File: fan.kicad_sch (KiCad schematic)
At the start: 9 parts, among them J6 Conn_01x04, U11 EMC2101

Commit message: migrated over lots of bitaxe parts to blockaxe
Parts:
- J6: footprint bitaxe:470531000 -> blockaxe:470531000
- U11: symbol bitaxe:EMC2101 -> blockaxe:EMC2101
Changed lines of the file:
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@@
       (effects (font (size 1.27 1.27)) hide)
     )
-    (property "Footprint" "bitaxe:470531000" (at 177.8 107.95 0)
+    (property "Footprint" "blockaxe:470531000" (at 177.8 107.95 0)
       (effects (font (size 1.27 1.27)) hide)
     )
@@
     )
   )
-  (symbol (lib_id "bitaxe:EMC2101") (at 139.065 72.39 0) (unit 1)
+  (symbol (lib_id "blockaxe:EMC2101") (at 139.065 72.39 0) (unit 1)
     (in_bom yes) (on_board yes) (dnp no)
     (property "Reference" "U11" (at 147.955 63.5 0)

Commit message: finished routing. switched back to THT barrel
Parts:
- TP13, TP14: footprint TestPoint:TestPoint_Pad_D1.5mm -> TestPoint:TestPoint_Pad_D1.0mm
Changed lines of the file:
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@@
       (effects (font (size 1.27 1.27)) (justify left) hide)
     )
-    (property "Footprint" "TestPoint:TestPoint_Pad_D1.5mm" (at 129.54 110.49 0)
+    (property "Footprint" "TestPoint:TestPoint_Pad_D1.0mm" (at 129.54 110.49 0)
       (effects (font (size 1.27 1.27)) hide)
     )
@@
       (effects (font (size 1.27 1.27)) (justify left) hide)
     )
-    (property "Footprint" "TestPoint:TestPoint_Pad_D1.5mm" (at 163.195 107.95 0)
+    (property "Footprint" "TestPoint:TestPoint_Pad_D1.0mm" (at 163.195 107.95 0)
       (effects (font (size 1.27 1.27)) hide)
     )

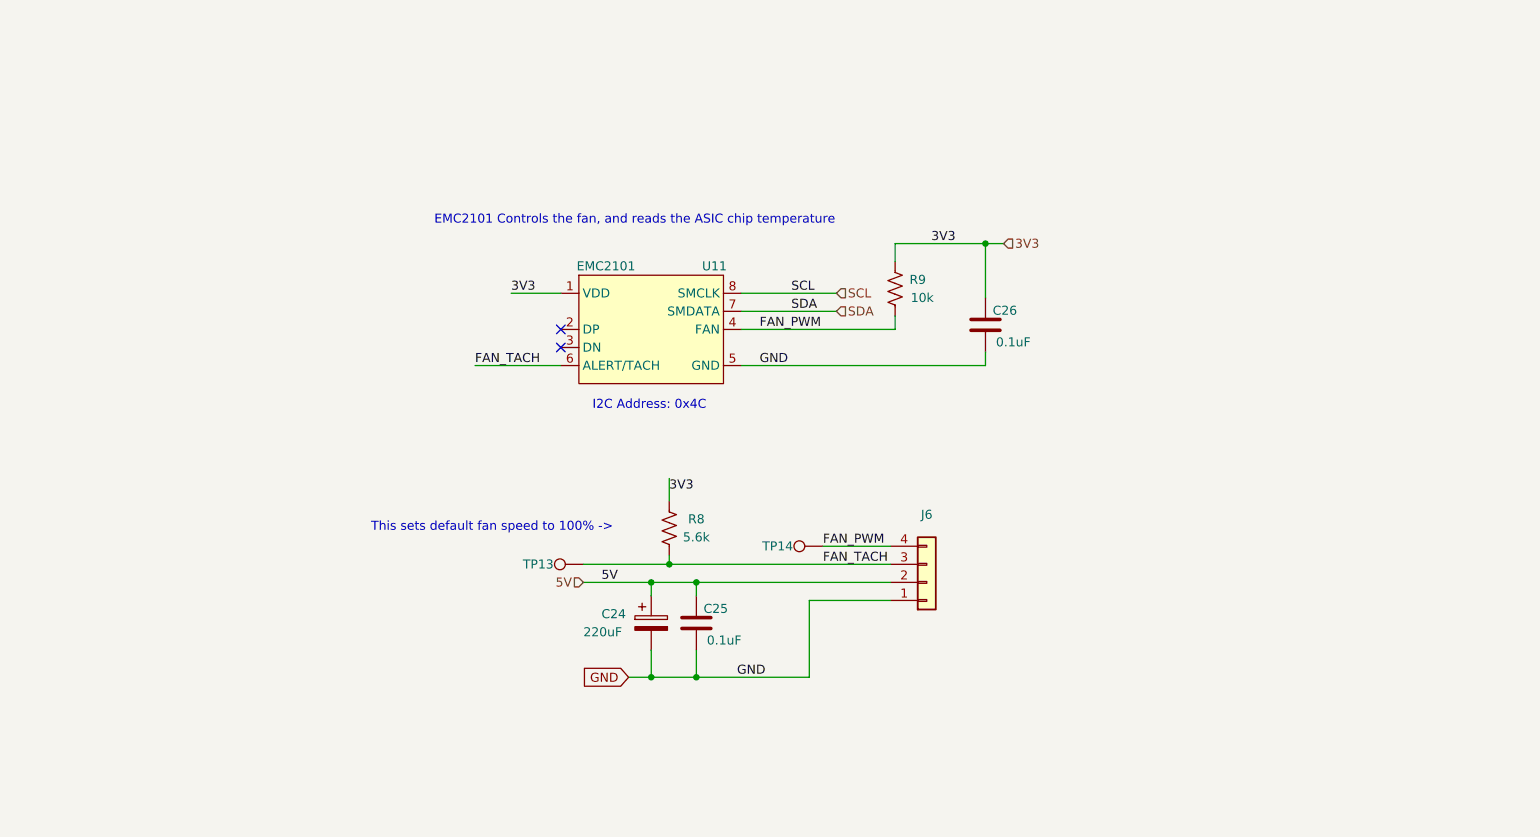
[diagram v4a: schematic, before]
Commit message: switch to bitaxeAura/GT base
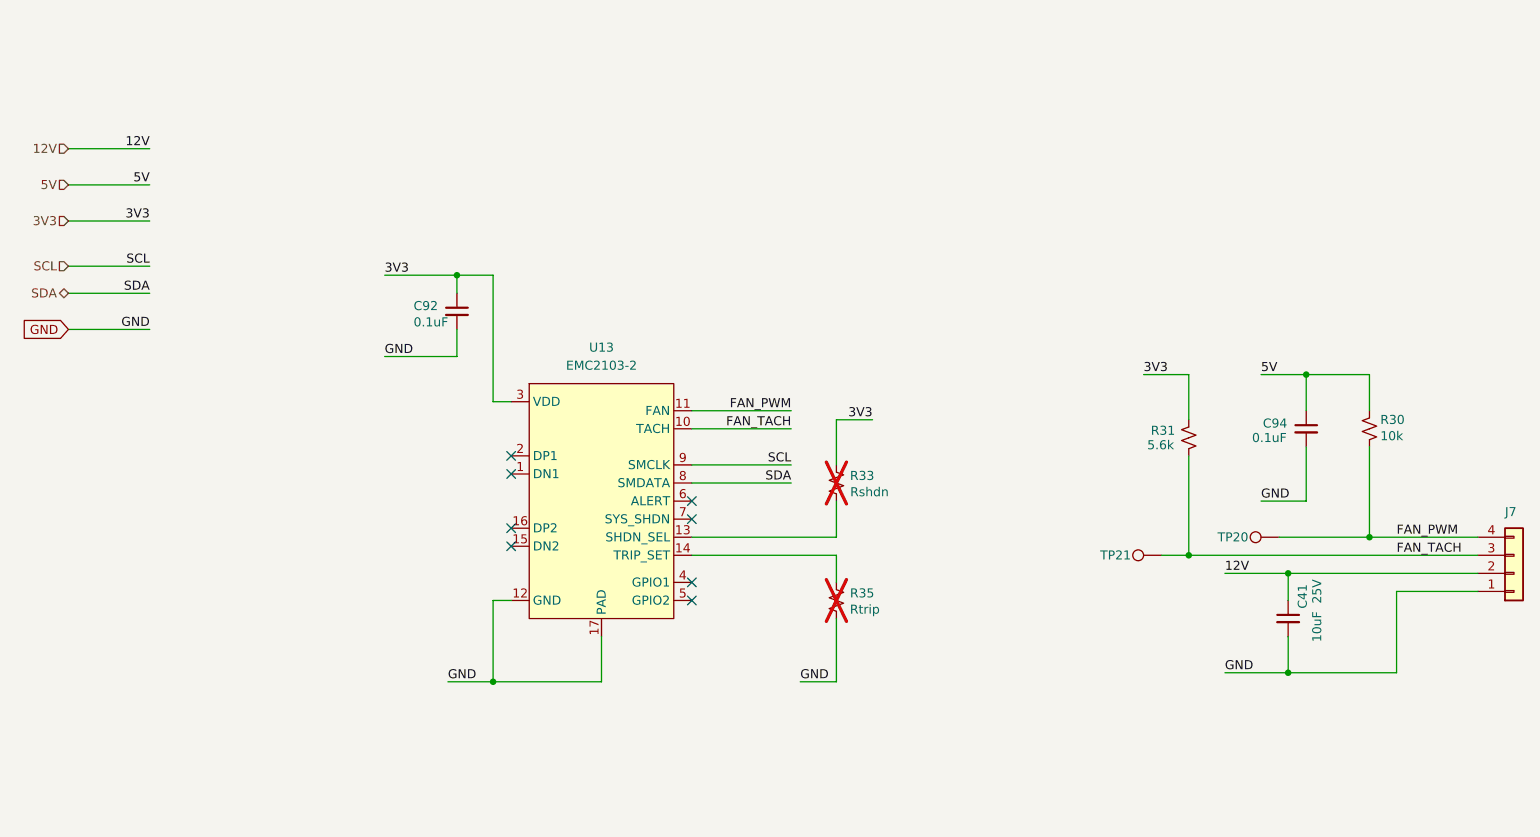
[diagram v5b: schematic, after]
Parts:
- removed C24: 220uF, Capacitor_SMD:CP_Elec_6.3x7.7, symbol Device:C_Polarized
- removed C25, C26: 0.1uF, Capacitor_SMD:C_0402_1005Metric, symbol Device:C
- removed J6: Conn_01x04, blockaxe:470531000, symbol Connector_Generic:Conn_01x04
- removed R8: 5.6k, Resistor_SMD:R_0402_1005Metric, symbol Device:R_US
- removed R9: 10k, Resistor_SMD:R_0402_1005Metric, symbol Device:R_US
- removed TP13, TP14: TestPoint, TestPoint:TestPoint_Pad_D1.0mm, symbol Connector:TestPoint
- removed U11: EMC2101, Package_SO:TSSOP-8_3x3mm_P0.65mm, symbol blockaxe:EMC2101
- added C41: 10uF, Capacitor_SMD:C_0603_1608Metric, symbol Device:C_Small
- added C92, C94: 0.1uF, Capacitor_SMD:C_0402_1005Metric, symbol Device:C_Small
- added J7: Conn_01x04, bitaxe:470531000, symbol Connector_Generic:Conn_01x04
- added R30: 10k, Resistor_SMD:R_0402_1005Metric, symbol Device:R_Small_US
- added R31: 5.6k, Resistor_SMD:R_0402_1005Metric, symbol Device:R_Small_US
- added R33: Rshdn, Resistor_SMD:R_0402_1005Metric, symbol Device:R_Small_US
- added R35: Rtrip, Resistor_SMD:R_0402_1005Metric, symbol Device:R_Small_US
- added TP20, TP21: TestPoint, TestPoint:TestPoint_Pad_D1.0mm, symbol Connector:TestPoint
- added U13: EMC2103-2, Package_DFN_QFN:QFN-16-1EP_4x4mm_P0.65mm_EP2.1x2.1mm, symbol bitaxe:EMC2103-2
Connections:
- net 3V3: now also C92.1, R31.2, R33.2, U13.3 (VDD)
- net 5V: now also C94.1, R30.2
- net FAN_PWM: now also J7.4 (Pin_4), R30.1, TP20.1, U13.11 (FAN)
- net FAN_TACH: now also J7.3 (Pin_3), R31.1, TP21.1, U13.10 (TACH)
- net GND: now also C41.2, C92.2, C94.2, J7.1 (Pin_1), R35.1, U13.12 (GND), U13.17 (PAD)
- net SCL: now also U13.9 (SMCLK)
- net SDA: now also U13.8 (SMDATA)
- new net: R35.2, U13.14 (TRIP_SET)
- new net: R33.1, U13.13 (SHDN_SEL)
- new net 12V: C41.1, J7.2 (Pin_2)
- no-connect marks 2 -> 8
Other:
- note removed: "EMC2101 Controls the fan, and reads the ASIC chip temperature"
- note removed: "I2C Address: 0x4C"
- note removed: "This sets default fan speed to 100% ->"
- title: blockaxe1 -> bitaxeBonanza

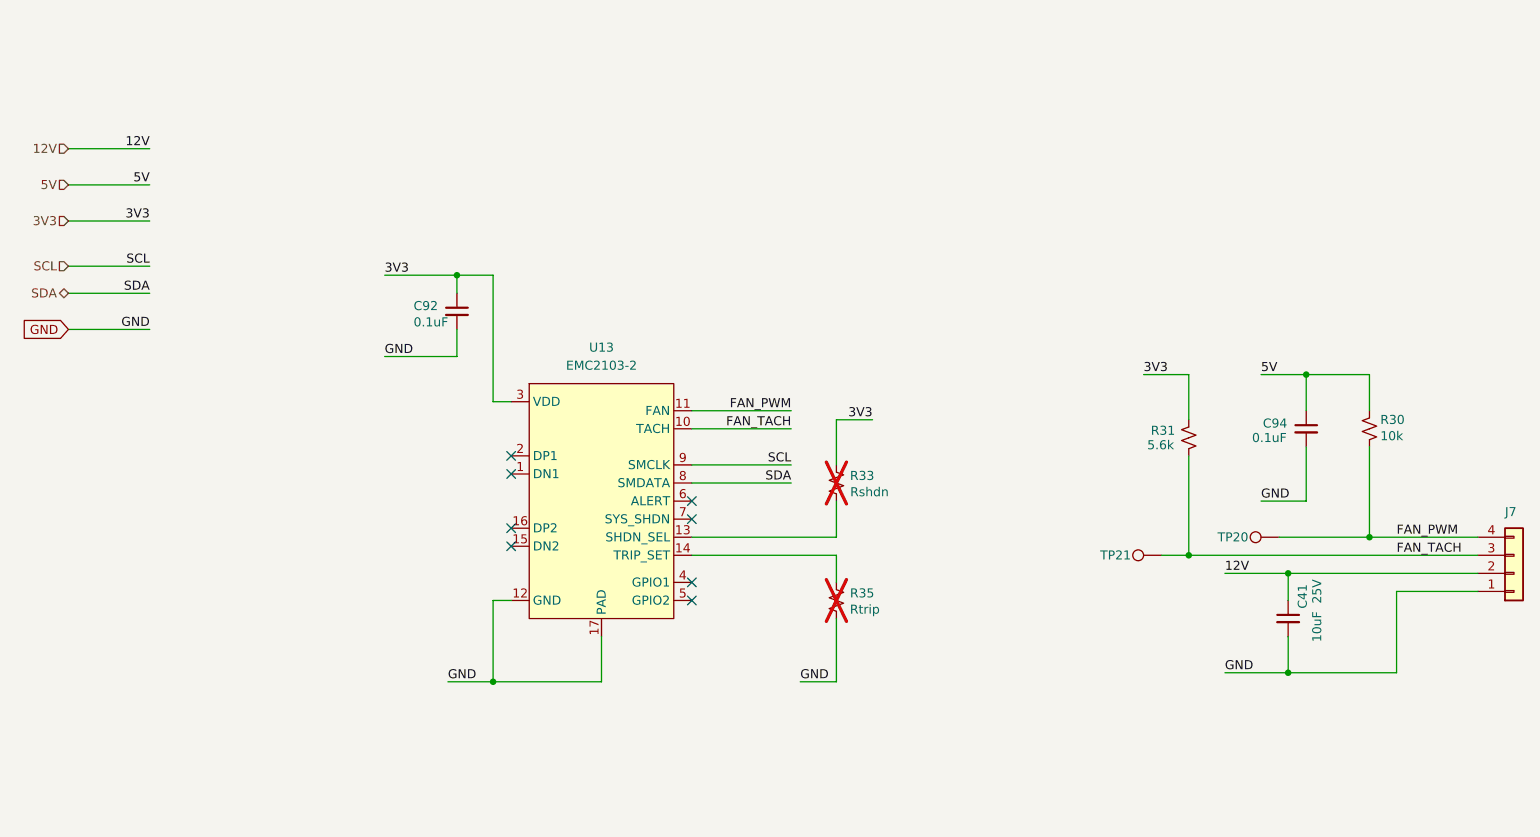
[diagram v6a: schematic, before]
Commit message: made the board double wide. rough ASIC and vreg placement.
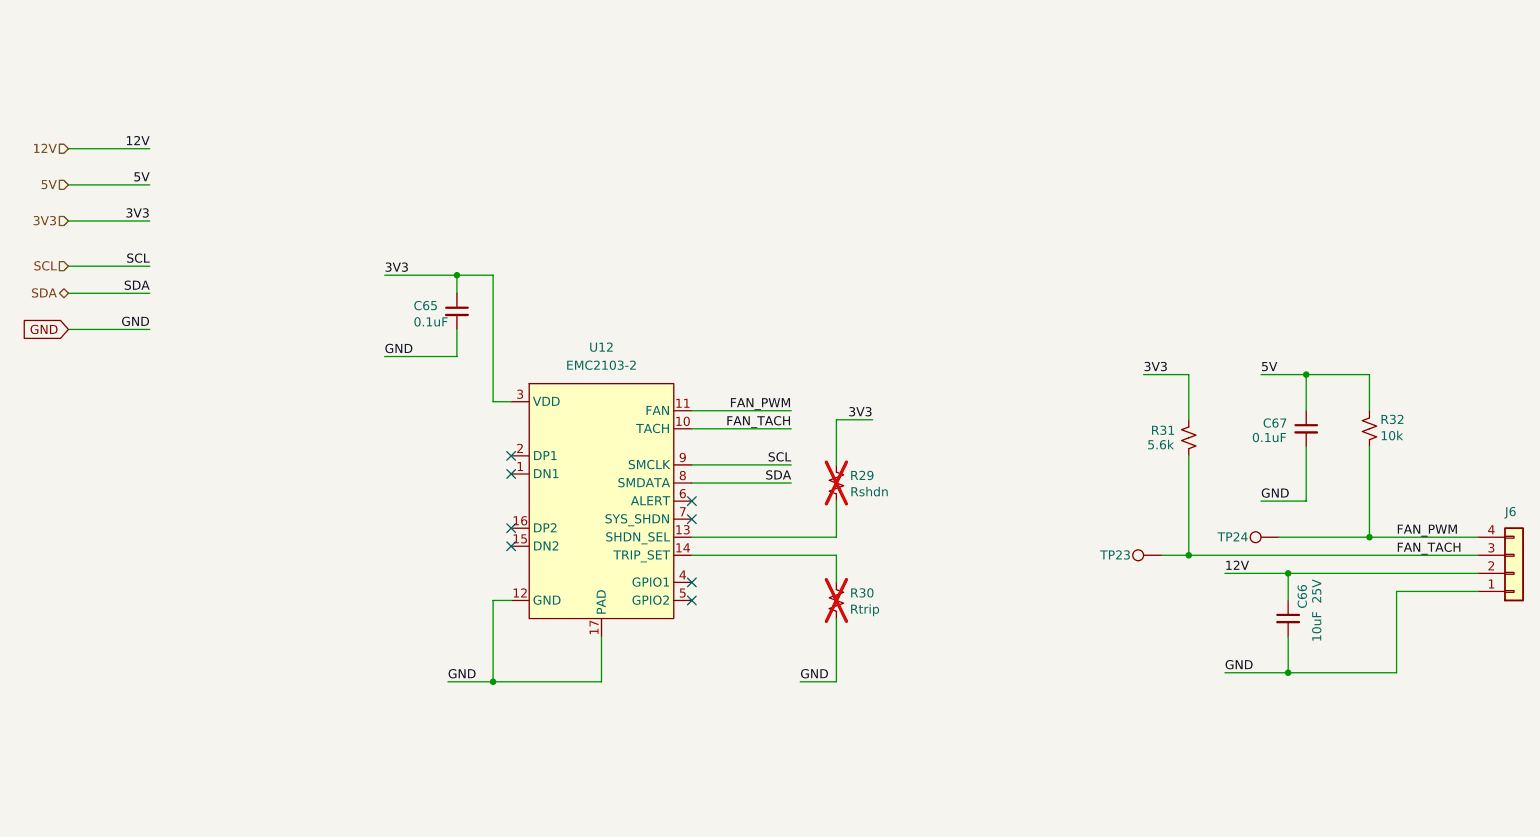
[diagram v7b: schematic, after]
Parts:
- renumbered C92 to C65, C41 to C66, C94 to C67, J7 to J6, R33 to R29, R35 to R30, R30 to R32, TP21 to TP23, TP20 to TP24, U13 to U12
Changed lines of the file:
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@@
 		(on_board yes)
 		(dnp no)
-		(property "Reference" "TP21"
+		(property "Reference" "TP23"
 			(at 206.502 104.14 90)
 			(effects
@@
 			(project "BitaxeGT"
 				(path "/61fe8d2c-9301-4ad9-8caf-c47acfa835b0/edab3562-ad75-4c4e-afab-a1841dcf5714"
-					(reference "TP21")
+					(reference "TP23")
 					(unit 1)
 				)
@@
 		(on_board yes)
 		(dnp yes)
-		(property "Reference" "R35"
+		(property "Reference" "R30"
 			(at 170.434 109.474 0)
 			(effects
@@
 			(project "BitaxeGT"
 				(path "/61fe8d2c-9301-4ad9-8caf-c47acfa835b0/edab3562-ad75-4c4e-afab-a1841dcf5714"
-					(reference "R35")
+					(reference "R30")
 					(unit 1)
 				)
@@
 		(dnp no)
 		(fields_autoplaced yes)
-		(property "Reference" "U13"
+		(property "Reference" "U12"
 			(at 132.08 74.93 0)
 			(effects
@@
 			(project ""
 				(path "/61fe8d2c-9301-4ad9-8caf-c47acfa835b0/edab3562-ad75-4c4e-afab-a1841dcf5714"
-					(reference "U13")
+					(reference "U12")
 					(unit 1)
 				)
@@
 		(on_board yes)
 		(dnp yes)
-		(property "Reference" "R33"
+		(property "Reference" "R29"
 			(at 170.434 92.964 0)
 			(effects
@@
 			(project "BitaxeGT"
 				(path "/61fe8d2c-9301-4ad9-8caf-c47acfa835b0/edab3562-ad75-4c4e-afab-a1841dcf5714"
-					(reference "R33")
+					(reference "R29")
 					(unit 1)
 				)
@@
 		(on_board yes)
 		(dnp no)
-		(property "Reference" "R30"
+		(property "Reference" "R32"
 			(at 241.554 85.09 0)
 			(effects
@@
 			(project "BitaxeGT"
 				(path "/61fe8d2c-9301-4ad9-8caf-c47acfa835b0/edab3562-ad75-4c4e-afab-a1841dcf5714"
-					(reference "R30")
+					(reference "R32")
 					(unit 1)
 				)
@@
 		(on_board yes)
 		(dnp no)
-		(property "Reference" "TP20"
+		(property "Reference" "TP24"
 			(at 223.012 101.6 90)
 			(effects
@@
 			(project "BitaxeGT"
 				(path "/61fe8d2c-9301-4ad9-8caf-c47acfa835b0/edab3562-ad75-4c4e-afab-a1841dcf5714"
-					(reference "TP20")
+					(reference "TP24")
 					(unit 1)
 				)
@@
 		(on_board yes)
 		(dnp no)
-		(property "Reference" "J7"
+		(property "Reference" "J6"
 			(at 259.08 98.044 0)
 			(effects
@@
 			(project "BitaxeGT"
 				(path "/61fe8d2c-9301-4ad9-8caf-c47acfa835b0/edab3562-ad75-4c4e-afab-a1841dcf5714"
-					(reference "J7")
+					(reference "J6")
 					(unit 1)
 				)
@@
 		(on_board yes)
 		(dnp no)
-		(property "Reference" "C92"
+		(property "Reference" "C65"
 			(at 105.664 69.088 0)
 			(effects
@@
 			(project "BitaxeGT"
 				(path "/61fe8d2c-9301-4ad9-8caf-c47acfa835b0/edab3562-ad75-4c4e-afab-a1841dcf5714"
-					(reference "C92")
+					(reference "C65")
 					(unit 1)
 				)
@@
 		(on_board yes)
 		(dnp no)
-		(property "Reference" "C94"
+		(property "Reference" "C67"
 			(at 225.044 85.598 0)
 			(effects
@@
 			(project "BitaxeGT"
 				(path "/61fe8d2c-9301-4ad9-8caf-c47acfa835b0/edab3562-ad75-4c4e-afab-a1841dcf5714"
-					(reference "C94")
+					(reference "C67")
 					(unit 1)
 				)
@@
 		(on_board yes)
 		(dnp no)
-		(property "Reference" "C41"
+		(property "Reference" "C66"
 			(at 230.632 108.204 90)
 			(effects
@@
 			(project "BitaxeGT"
 				(path "/61fe8d2c-9301-4ad9-8caf-c47acfa835b0/edab3562-ad75-4c4e-afab-a1841dcf5714"
-					(reference "C41")
+					(reference "C66")
 					(unit 1)
 				)

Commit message: switch to EMC2302 for 2 fans and no temp sensor
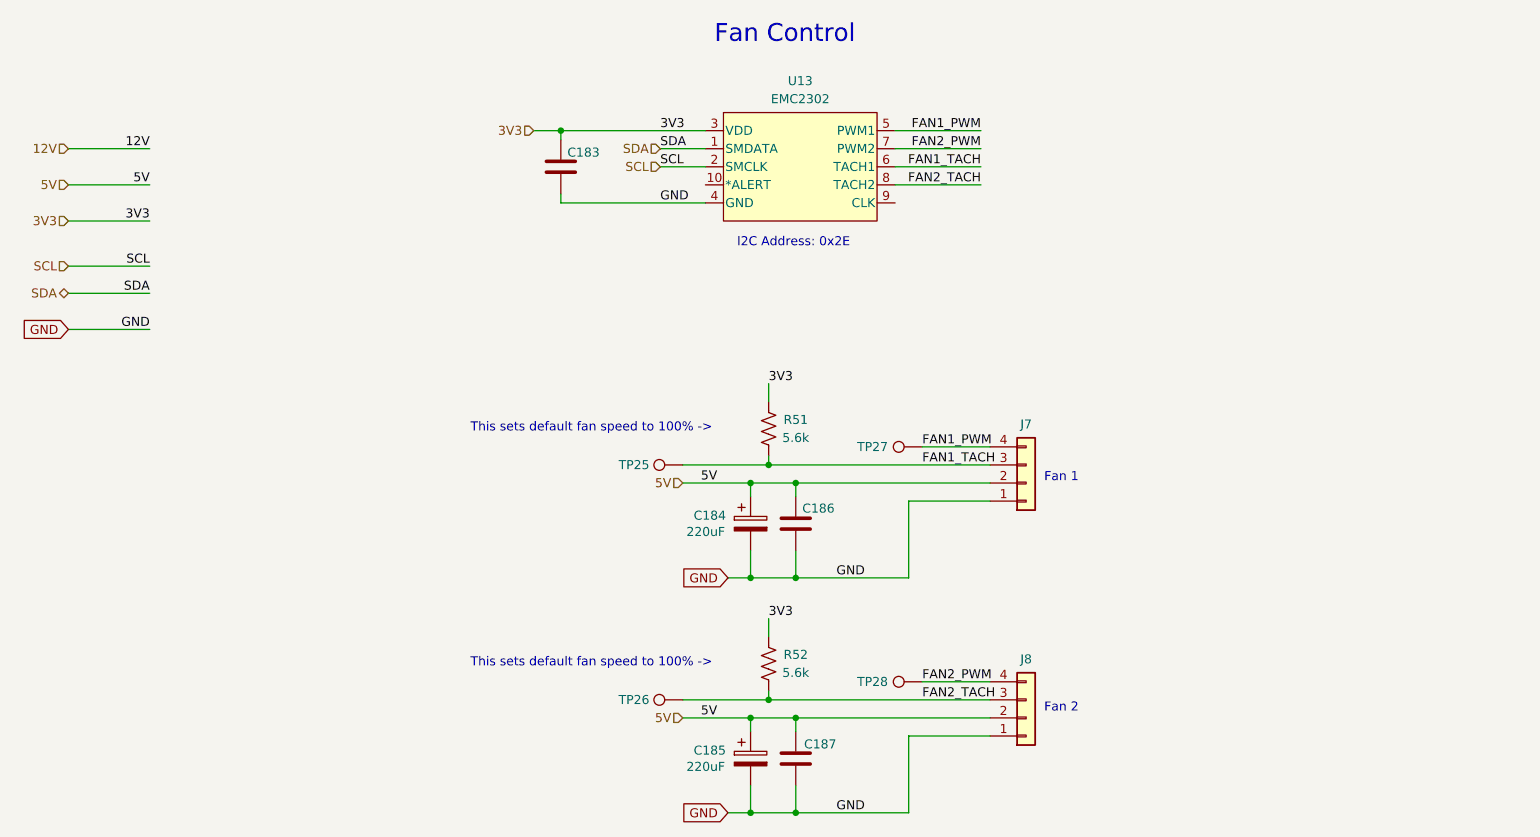
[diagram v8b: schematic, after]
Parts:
- removed C65, C67: 0.1uF, Capacitor_SMD:C_0402_1005Metric, symbol Device:C_Small
- removed C66: 10uF, Capacitor_SMD:C_0603_1608Metric, symbol Device:C_Small
- removed J6: Conn_01x04, bitaxe:470531000, symbol Connector_Generic:Conn_01x04
- removed R29: Rshdn, Resistor_SMD:R_0402_1005Metric, symbol Device:R_Small_US
- removed R30: Rtrip, Resistor_SMD:R_0402_1005Metric, symbol Device:R_Small_US
- removed R31: 5.6k, Resistor_SMD:R_0402_1005Metric, symbol Device:R_Small_US
- removed R32: 10k, Resistor_SMD:R_0402_1005Metric, symbol Device:R_Small_US
- removed TP23, TP24: TestPoint, TestPoint:TestPoint_Pad_D1.0mm, symbol Connector:TestPoint
- removed U12: EMC2103-2, Package_DFN_QFN:QFN-16-1EP_4x4mm_P0.65mm_EP2.1x2.1mm, symbol bitaxe:EMC2103-2
- added C183, C186, C187: 311-3342-1-ND, Capacitor_SMD:C_0402_1005Metric, symbol Device:C
- added C184, C185: 220uF, Capacitor_SMD:CP_Elec_6.3x7.7, symbol Device:C_Polarized
- added J7, J8: Conn_01x04, bitaxe:470531000, symbol Connector_Generic:Conn_01x04
- added R51, R52: 5.6k, Resistor_SMD:R_0402_1005Metric, symbol Device:R_US
- added TP25, TP26, TP27, TP28: TestPoint, TestPoint:TestPoint_Pad_D1.0mm, symbol Connector:TestPoint
- added U13: EMC2302, Package_SO:MSOP-10_3x3mm_P0.5mm, symbol bitaxe:EMC2302-2-AIZL-TR
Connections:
- net 3V3: now also C183.1, R51.2, R52.2, U13.3 (VDD)
- net 5V: now also C184.1, C185.1, C186.1, C187.1, J7.2 (Pin_2), J8.2 (Pin_2)
- net GND: now also C183.2, C184.2, C185.2, C186.2, C187.2, J7.1 (Pin_1), J8.1 (Pin_1), U13.4 (GND)
- net SCL: now also U13.2 (SMCLK)
- net SDA: now also U13.1 (SMDATA)
- new net FAN1_PWM: J7.4 (Pin_4), TP27.1, U13.5 (PWM1)
- new net FAN1_TACH: J7.3 (Pin_3), R51.1, TP25.1, U13.6 (TACH1)
- new net FAN2_PWM: J8.4 (Pin_4), TP28.1, U13.7 (PWM2)
- new net FAN2_TACH: J8.3 (Pin_3), R52.1, TP26.1, U13.8 (TACH2)
- no-connect marks 8 -> 0
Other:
- note added: "Fan 1"
- note added: "Fan 2"
- note added: "Fan Control"
- note added: "I2C Address: 0x2E"
- note added: "This sets default fan speed to 100% ->"
